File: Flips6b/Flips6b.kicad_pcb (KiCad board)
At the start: 2 copper layers, 90 x 50 mm, 28 parts, among them CN201 Conn_02x05_Odd_Even, CN301 Conn_02x05_Odd_Even, CN401 Conn_02x05_Odd_Even, CN501 Conn_02x05_Odd_Even, CN601 Conn_02x05_Odd_Even, CN701 Conn_02x05_Odd_Even, CN801 Conn_02x05_Odd_Even, J101 Conn_02x04_Odd_Even, U201 74HCT595, U301 74HCT595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

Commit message: first attempt of Flips6b
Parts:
- removed C201, C301, C401, C501, C601, C701, C801: 0u1, Capacitors_SMD:C_0805_HandSoldering
- removed CN201, CN301, CN401, CN501, CN601, CN701, CN801: Conn_02x05_Odd_Even, Socket_Strips:Socket_Strip_Straight_2x05_Pitch2.54mm
- removed J101: Conn_02x04_Odd_Even, Socket_Strips:Socket_Strip_Straight_2x04_Pitch2.54mm
- removed R101, R102: 10K, Resistors_SMD:R_0805_HandSoldering
- removed REF** (x4): MountingHole_3.2mm_M3_DIN965_Pad, Mounting_Holes:MountingHole_3.2mm_M3_DIN965_Pad
- removed U201, U301, U401, U501, U601, U701, U801: 74HCT595, SMD_Packages:SO-16-N
- added C1: 0u1, Capacitors_SMD:C_0805_HandSoldering, F.Cu at (184.8, 63.5)
- added C2: 0u1, Capacitors_SMD:C_0805_HandSoldering, F.Cu at (225.4, 63.5)
- added C3: 0u1, Capacitors_SMD:C_0805_HandSoldering, F.Cu at (207.0, 63.5)
- added C4: 0u1, Capacitors_SMD:C_0805_HandSoldering, F.Cu at (248.3, 63.5)
- added CN1: Conn_02x04_Odd_Even, Socket_Strips:Socket_Strip_Straight_2x04_Pitch2.54mm, F.Cu at (182.9, 94.0)
- added CNX1: Conn_02x05_Odd_Even, Socket_Strips:Socket_Strip_Straight_2x05_Pitch2.54mm, F.Cu at (213.4, 94.0)
- added CNX2: Conn_02x05_Odd_Even, Socket_Strips:Socket_Strip_Straight_2x05_Pitch2.54mm, F.Cu at (223.5, 94.0)
- added CNX3: Conn_02x05_Odd_Even, Socket_Strips:Socket_Strip_Straight_2x05_Pitch2.54mm, F.Cu at (233.7, 94.0)
- added CNX4: Conn_02x05_Odd_Even, Socket_Strips:Socket_Strip_Straight_2x05_Pitch2.54mm, F.Cu at (243.8, 94.0)
- added CNX5: Conn_02x05_Odd_Even, Socket_Strips:Socket_Strip_Straight_2x05_Pitch2.54mm, F.Cu at (254.0, 94.0)
- added CNY1: Conn_02x05_Odd_Even, Socket_Strips:Socket_Strip_Straight_2x05_Pitch2.54mm, F.Cu at (193.0, 94.0)
- added CNY2: Conn_02x05_Odd_Even, Socket_Strips:Socket_Strip_Straight_2x05_Pitch2.54mm, F.Cu at (203.2, 94.0)
- added R1: 10K, Resistors_SMD:R_0805_HandSoldering, F.Cu at (184.1, 98.4)
- added R2: 10K, Resistors_SMD:R_0805_HandSoldering, F.Cu at (180.3, 75.6)
- added U1: 74HCT595, SMD_Packages:SO-16-N, F.Cu at (189.2, 71.8)
- added U2: 74HCT595, SMD_Packages:SO-16-N, F.Cu at (229.9, 71.8)
- added U3: 74HC238, SMD_Packages:SO-16-N, F.Cu at (203.8, 71.8)
- added U4: 74HC238, SMD_Packages:SO-16-N, F.Cu at (245.1, 71.8)
- added U5: 74LVC1G04, TO_SOT_Packages_SMD:SOT-23-5, F.Cu at (215.3, 71.8)
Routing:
- net ~SRCLR: track 109.7 -> 0.00 mm, vias 7 -> 0
- net ~OE: track 107.8 -> 0.00 mm, vias 8 -> 0
- net SRCLK: track 98.1 -> 0.00 mm, vias 7 -> 0
- net /ENABLE: track 0.00 -> 93.3 mm, vias 0 -> 4
- net RCLK: track 89.5 -> 0.00 mm, vias 7 -> 0
- net /XA2: track 0.00 -> 81.9 mm, vias 0 -> 5
- net /XA0: track 0.00 -> 74.8 mm, vias 0 -> 1
- net /XB1: track 0.00 -> 64.4 mm, vias 0 -> 4
- net /XA1: track 0.00 -> 62.3 mm, vias 0 -> 1
- net /XE.0: track 0.00 -> 59.0 mm, vias 0 -> 2
- net /XD: track 0.00 -> 58.5 mm, vias 0 -> 1
- net /~SRCLR: track 0.00 -> 56.4 mm, vias 0 -> 2
- net /XB0: track 0.00 -> 54.7 mm, vias 0 -> 1
- net /SRCLK: track 0.00 -> 46.6 mm, vias 0 -> 2
- net /XE.1: track 0.00 -> 45.8 mm, vias 0 -> 2
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
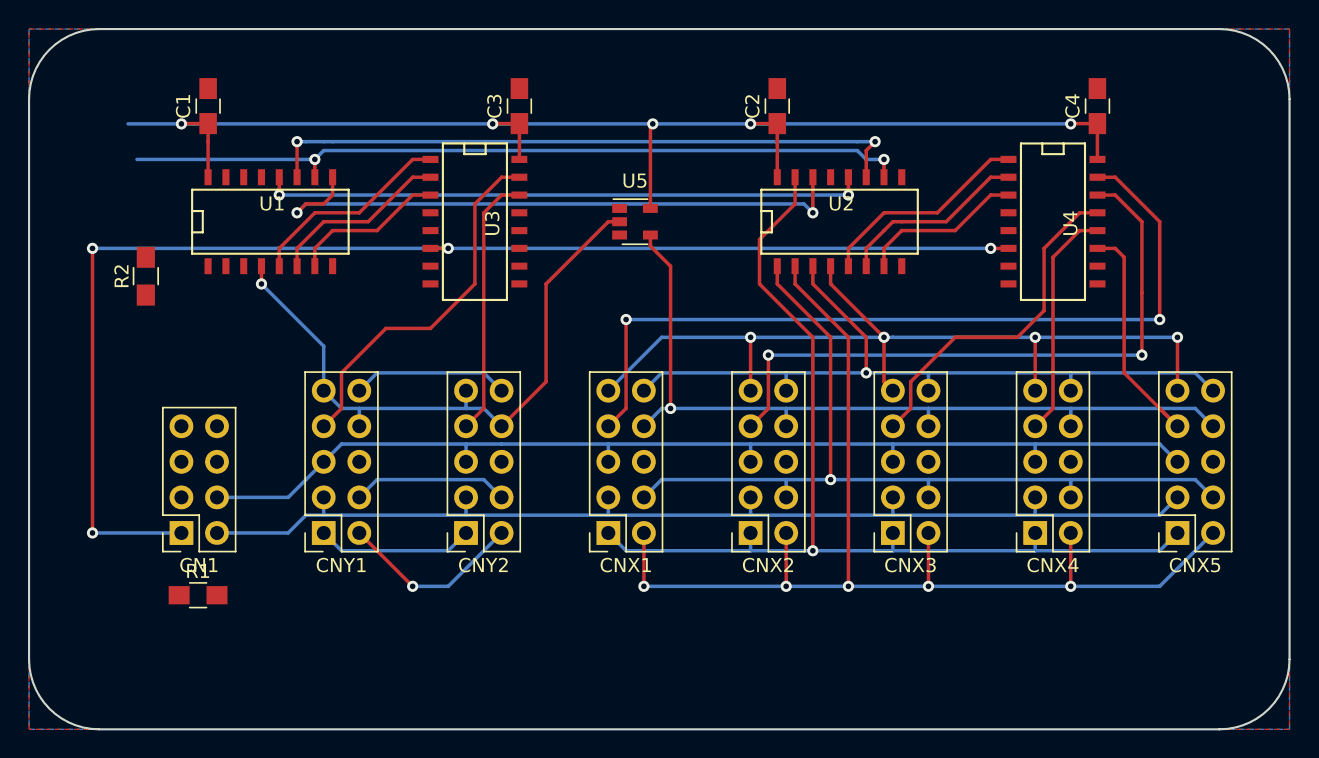
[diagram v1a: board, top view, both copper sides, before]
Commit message: first attempt for Flips6b routed
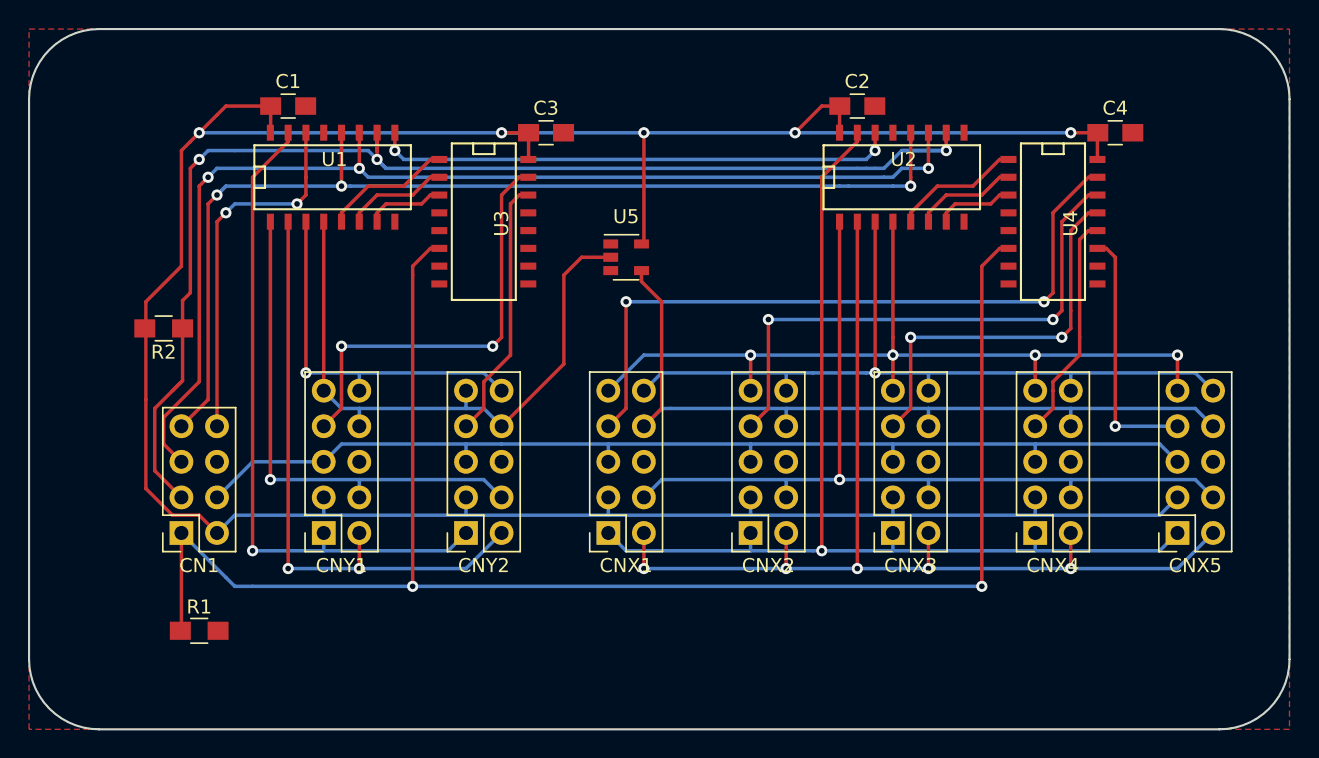
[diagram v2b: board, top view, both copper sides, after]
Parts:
- moved C1 5.72 mm to (190.5, 63.5), turned to 0 degrees
- moved C2 5.71 mm to (231.1, 63.5), turned to 0 degrees
- moved U1 5.46 mm to (193.7, 68.6)
- moved U2 5.46 mm to (234.3, 68.6)
- moved R2 3.94 mm to (181.6, 79.4), turned to 180 degrees
- moved C3 2.69 mm to (208.9, 65.4), turned to 0 degrees
- moved U5 2.62 mm to (214.6, 74.3)
- moved R1 2.54 mm to (184.2, 101.0)
- moved C4 2.29 mm to (249.6, 65.4), turned to 0 degrees
- moved U3 0.63 mm to (204.5, 71.8)
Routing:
- net /YA0: track 11.2 -> 47.9 mm, vias 0 -> 1
- net /~SRCLR: track 56.4 -> 90.9 mm, vias 2 -> 3
- net /RCLK: track 43.2 -> 76.5 mm, vias 2 -> 3
- net /SRCLK: track 46.6 -> 79.5 mm, vias 2 -> 3
- net +5V: track 171.1 -> 202.2 mm
- net /YA2: track 13.3 -> 43.6 mm, vias 1 -> 2
- net /DIN: track 0.00 -> 26.2 mm, vias 0 -> 2
- net /YA1: track 11.2 -> 36.7 mm, vias 0 -> 1
- net /ENABLE: track 93.3 -> 116.3 mm, vias 4 -> 2
- net /YB0: track 11.2 -> 26.6 mm, vias 0 -> 1
- net /XE.0: track 59.0 -> 50.1 mm
- net Net-(U1-Pad9): track 44.2 -> 37.4 mm
- net /XE.1: track 45.8 -> 39.0 mm
- net /XC2: track 11.7 -> 5.61 mm
- net /XC1: track 13.5 -> 7.40 mm
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- removed copper zone on B.Cu, net GND

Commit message: adding vias to Flips6b
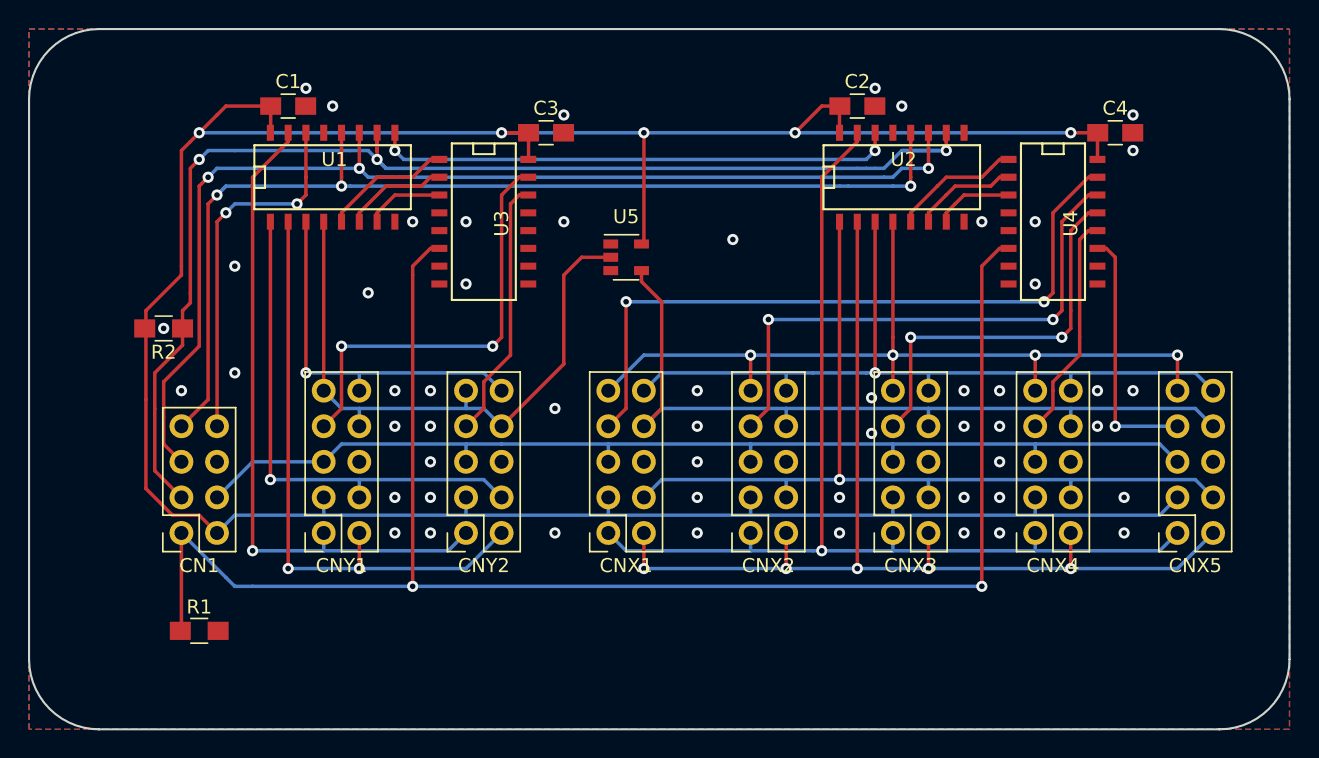
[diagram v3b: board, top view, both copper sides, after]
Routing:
- net /~SRCLR: track 90.9 -> 90.0 mm
- net GND: vias 0 -> 54
- added copper zone on B.Cu, net GND

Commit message: Rudimentary silk screen
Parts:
- added REF**: MountingHole_3.2mm_M3_DIN965_Pad, Mounting_Holes:MountingHole_3.2mm_M3_DIN965_Pad, F.Cu at (257.0, 63.0)
- added REF**: MountingHole_3.2mm_M3_DIN965_Pad, Mounting_Holes:MountingHole_3.2mm_M3_DIN965_Pad, F.Cu at (177.0, 63.0)
- added REF**: MountingHole_3.2mm_M3_DIN965_Pad, Mounting_Holes:MountingHole_3.2mm_M3_DIN965_Pad, F.Cu at (177.0, 103.0)
- added REF**: MountingHole_3.2mm_M3_DIN965_Pad, Mounting_Holes:MountingHole_3.2mm_M3_DIN965_Pad, F.Cu at (257.0, 103.0)
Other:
- board text added: "Flips 6b"
